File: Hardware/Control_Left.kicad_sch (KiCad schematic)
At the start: 0 parts

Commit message: Schematic review
Initial shcematic iteration.
Added all footprints and part numbers.
Only a quick review was performed.
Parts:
- added C1, C5, C6: 1u, Capacitor_SMD:C_0603_1608Metric, symbol Device:C
- added C2, C4: 4.7u, Capacitor_SMD:C_1206_3216Metric, symbol Device:C
- added C3: 10p, Capacitor_SMD:C_0603_1608Metric, symbol Device:C
- added D1, D2, D3: DSK24, Diode_SMD:D_SOD-123F, symbol Device:D_Schottky
- added J1: BAT, Custom_Parts:JST_PH_1x02_P2.00MM_SMD_HOR, symbol Connector_Generic_MountingPin:Conn_01x02_MountingPin
- added J2: TagConnect, Connector:Tag-Connect_TC2030-IDC-NL_2x03_P1.27mm_Vertical, symbol Connector:Conn_ARM_SWD_TagConnect_TC2030-NL
- added J3: 0.96_TFT_MODULE, Custom_Parts:Jushuo_AFC07-S06FCA-00_1x8-1MP_P0.50_Horizontal, symbol Custom_Parts:0.96_TFT_MODULE
- added L1: 10u, Custom_Parts:VLCF4020, symbol Device:L
- added Q1, Q2: AO3401A, Package_TO_SOT_SMD:SOT-23, symbol Transistor_FET:AO3401A
- added R1: 100K, Resistor_SMD:R_0603_1608Metric, symbol Device:R
- added R2: 500, Resistor_SMD:R_0603_1608Metric, symbol Device:R
- added R3: 470K, Resistor_SMD:R_0603_1608Metric, symbol Device:R
- added R4: 150K, Resistor_SMD:R_0603_1608Metric, symbol Device:R
- added R5: 100, Resistor_SMD:R_0603_1608Metric, symbol Device:R
- added R6, R7: 10K, Resistor_SMD:R_0603_1608Metric, symbol Device:R
- added R8: 22, Resistor_SMD:R_0603_1608Metric, symbol Device:R
- added SW1: MSK12C02, Custom_Parts:MSK12C02, symbol Custom_Parts:MSK12C02
- added U1: TPS61040DBV, Package_TO_SOT_SMD:SOT-23-5, symbol Regulator_Switching:TPS61040DBV
- added U2: XIAO-NRF52840-PLUS, Custom_Parts:XIAO-NRF52840-PLUS-SMD, symbol Custom_Parts:XIAO-NRF52840-PLUS-SMD
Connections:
- new net: C2.1, D1.1 (K), L1.1, Q1.2 (S), U1.5 (VIN)
- new net: D2.2 (A), L1.2, U1.1 (SW)
- new net: C3.2, R3.2, R4.1, U1.3 (FB)
- new net: R2.1, U2.8 (P1.12_RX)
- new net: J1.1 (Pin_1), SW1.2 (B)
- new net: Q2.2 (S), R7.1, R8.1
- new net: J3.1 (LEDA), R8.2
- new net: Q2.1 (G), R5.2, R7.2
- new net 3V3L: C6.1, D3.1 (K), J2.1 (VCC), J3.7 (VDD), Q2.3 (D), R6.1, U2.12 (3V3_OUT)
- new net 5VL: C3.1, C4.1, D2.1 (K), R3.1
- new net COL1_L: U2.1 (P0.02_A0)
- new net COL2_L: U2.2 (P0.03_A1)
- new net COL3_L: U2.3 (P0.28_A2)
- new net COL4_L: U2.4 (P0.29_A3)
- new net COL5_L: U2.5 (P0.04_SDA)
- new net COL6_L: U2.6 (P0.05_SCL)
- new net COL7_L: U2.7 (P1.11_TX)
- new net GND: C1.2, C2.2, C4.2, C5.2, C6.2, J1.2 (Pin_2), J1.MP (MountPin), J2.5 (GND), J3.2 (GND), J3.MP, R1.2, R4.2, SW1.MP, U1.2 (GND), U2.13 (GND), U2.27 (GND), U2.29 (GND)
- new net LCD_BKL: R5.1, U2.21 (P1.03_D17)
- new net LCD_CS: J3.8 (CS), U2.22 (P1.05_D18)
- new net LCD_DC: J3.4 (DC), U2.10 (P1.14_MISO)
- new net LCD_MOSI: J3.5 (SDA), U2.11 (P1.15_MOSI)
- new net LCD_RES: C5.1, D3.2 (A), J3.3 (RES), R6.2
- new net LCD_SCK: J3.6 (SCK), U2.9 (P1.13_SCK)
- new net LED_DATA_L: R2.2
- new net LED_EN: U1.4 (EN), U2.23 (P1.07_D19)
- new net ROW1_L: U2.15 (P0.15_SDOUT)
- new net ROW2_L: U2.16 (P0.19_SCLK)
- new net ROW3_L: U2.17 (P1.01_LRCK)
- new net ROW4_L: U2.18 (P0.09_NFC1)
- new net ROW5_L: U2.19 (P0.10_NFC2)
- new net SWDCLK: J2.4 (SWCLK), U2.25 (SWDCLK)
- new net SWDIO: J2.2 (SWDIO), U2.24 (SWDIO)
- new net VBATL: Q1.3 (D), SW1.3 (C), U2.28 (VBAT)
- new net VBUSL: C1.1, D1.2 (A), Q1.1 (G), R1.1, U2.14 (VBUS)
- new net ~{RESET}: J2.3 (~{RESET}), U2.26 (CHIP_EN)
- no-connect marks 0 -> 3

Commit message: Net configurations
Added net labels.
Updated the PCB components.
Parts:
- removed R2: 500, Resistor_SMD:R_0603_1608Metric, symbol Device:R
- added R1: 500, Resistor_SMD:R_0603_1608Metric, symbol Device:R
- renumbered R1 to R2
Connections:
- net LED_DATA_L: now also R1.2
- net VREGL: now reaches C2.1, D1.1 (K), L1.1, Q1.2 (S), U1.5 (VIN)
- net VSWL: now reaches D2.2 (A), L1.2, U1.1 (SW)
- net VFBL: now reaches C3.2, R3.2, R4.1, U1.3 (FB)
- net LED_DATA: now reaches U2.8 (P1.12_RX)
- net LED_DATA: now also R1.1
- net VBAT: now reaches J1.1 (Pin_1), SW1.2 (B)
- net BKLD: now reaches Q2.2 (S), R7.1, R8.1
- net BKL: now reaches J3.1 (LEDA), R8.2
- net BKLG: now reaches Q2.1 (G), R5.2, R7.2
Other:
- moved on the sheet: R5, R8

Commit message: Initial layout
Configured the switch and LED initial layout.
Need to add the capacitors for the LEDs and the diodes for the switches.
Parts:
- added R3: 10K, Resistor_SMD:R_0603_1608Metric, symbol Device:R
- renumbered R3 to R4, R4 to R5, R5 to R6, R6 to R7, R7 to R8, R8 to R9
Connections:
- net COL7_L is gone; now on net LED_EN: U2.7 (P1.11_TX)
- net GND: now also R3.1
- net LED_EN: now also R3.2; no longer U2.23 (P1.07_D19)
- new net ROW6_L: U2.23 (P1.07_D19)

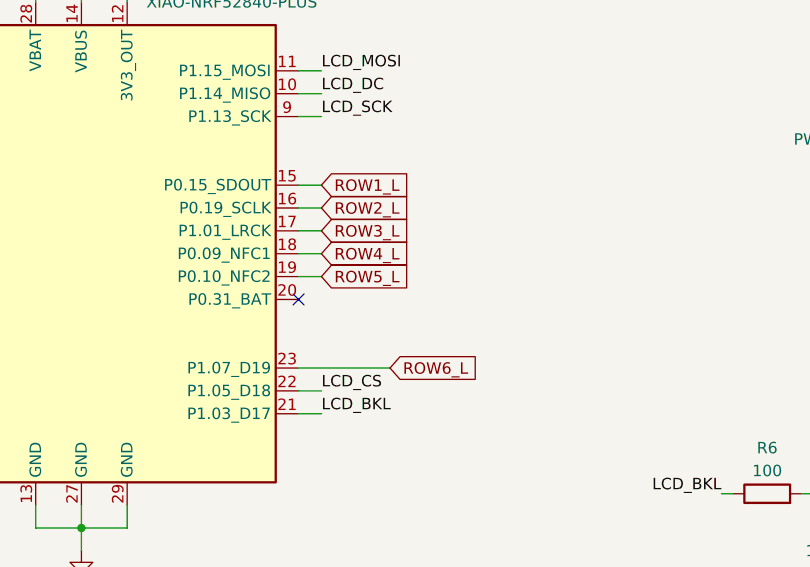
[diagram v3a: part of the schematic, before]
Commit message: Pin adjustment
Adjusted the pins for the encoders and other.
Now the battery measuring pin connected to an internal ADC on the XIAO nRF52840 also serves to read the rotation of the encoders.
Attention should be put as how to implement the BAT voltage measuring to check if the encoder is turning at the same time.
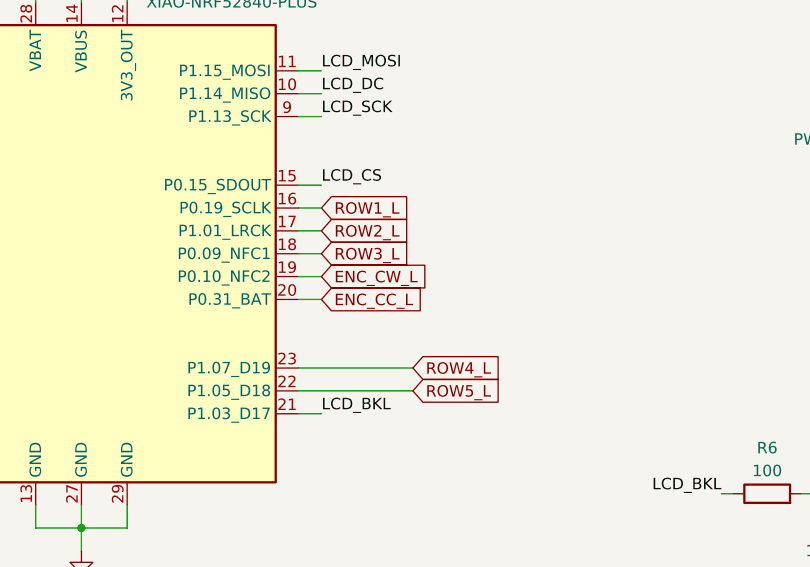
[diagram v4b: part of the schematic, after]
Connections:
- net ROW6_L is gone; now on net ROW4_L: U2.23 (P1.07_D19)
- net LCD_CS: now also U2.15 (P0.15_SDOUT); no longer U2.22 (P1.05_D18)
- net ROW1_L: now also U2.16 (P0.19_SCLK); no longer U2.15 (P0.15_SDOUT)
- net ROW2_L: now also U2.17 (P1.01_LRCK); no longer U2.16 (P0.19_SCLK)
- net ROW3_L: now also U2.18 (P0.09_NFC1); no longer U2.17 (P1.01_LRCK)
- net ROW4_L: no longer U2.18 (P0.09_NFC1)
- net ROW5_L: now also U2.22 (P1.05_D18); no longer U2.19 (P0.10_NFC2)
- net ENC_CC_L: now reaches U2.20 (P0.31_BAT)
- new net ENC_CW_L: U2.19 (P0.10_NFC2)
- no-connect marks 3 -> 2

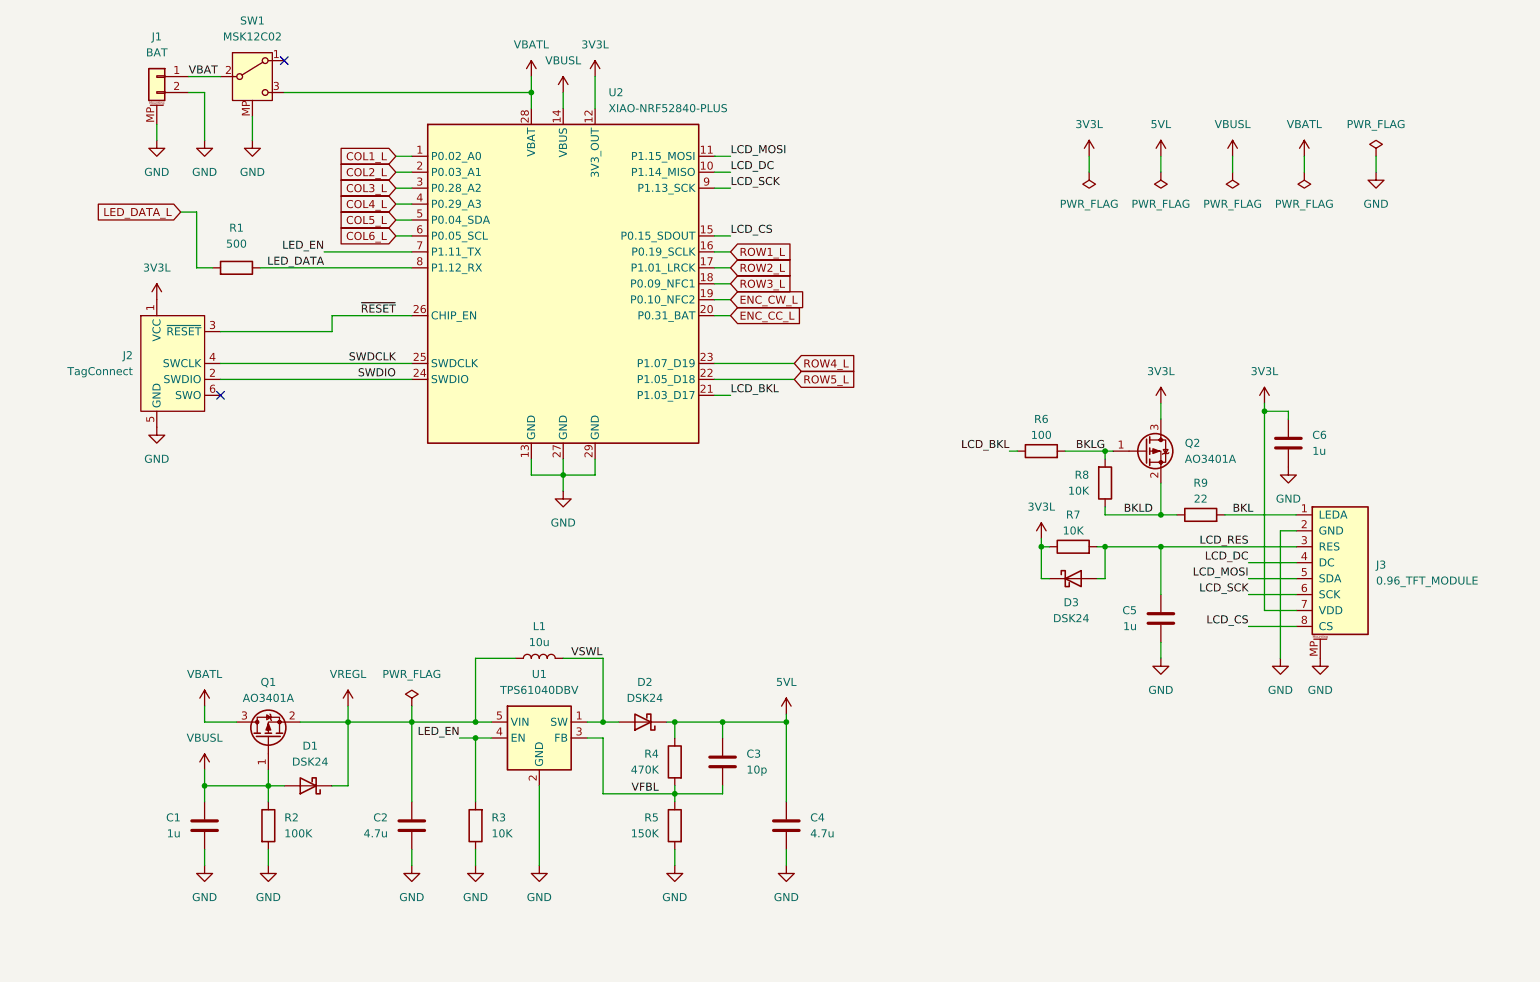
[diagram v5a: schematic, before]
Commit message: Key matrix and edges
Defined the key matrix locations and the board edges.
Next step: start routing and verify the buck converter layout.
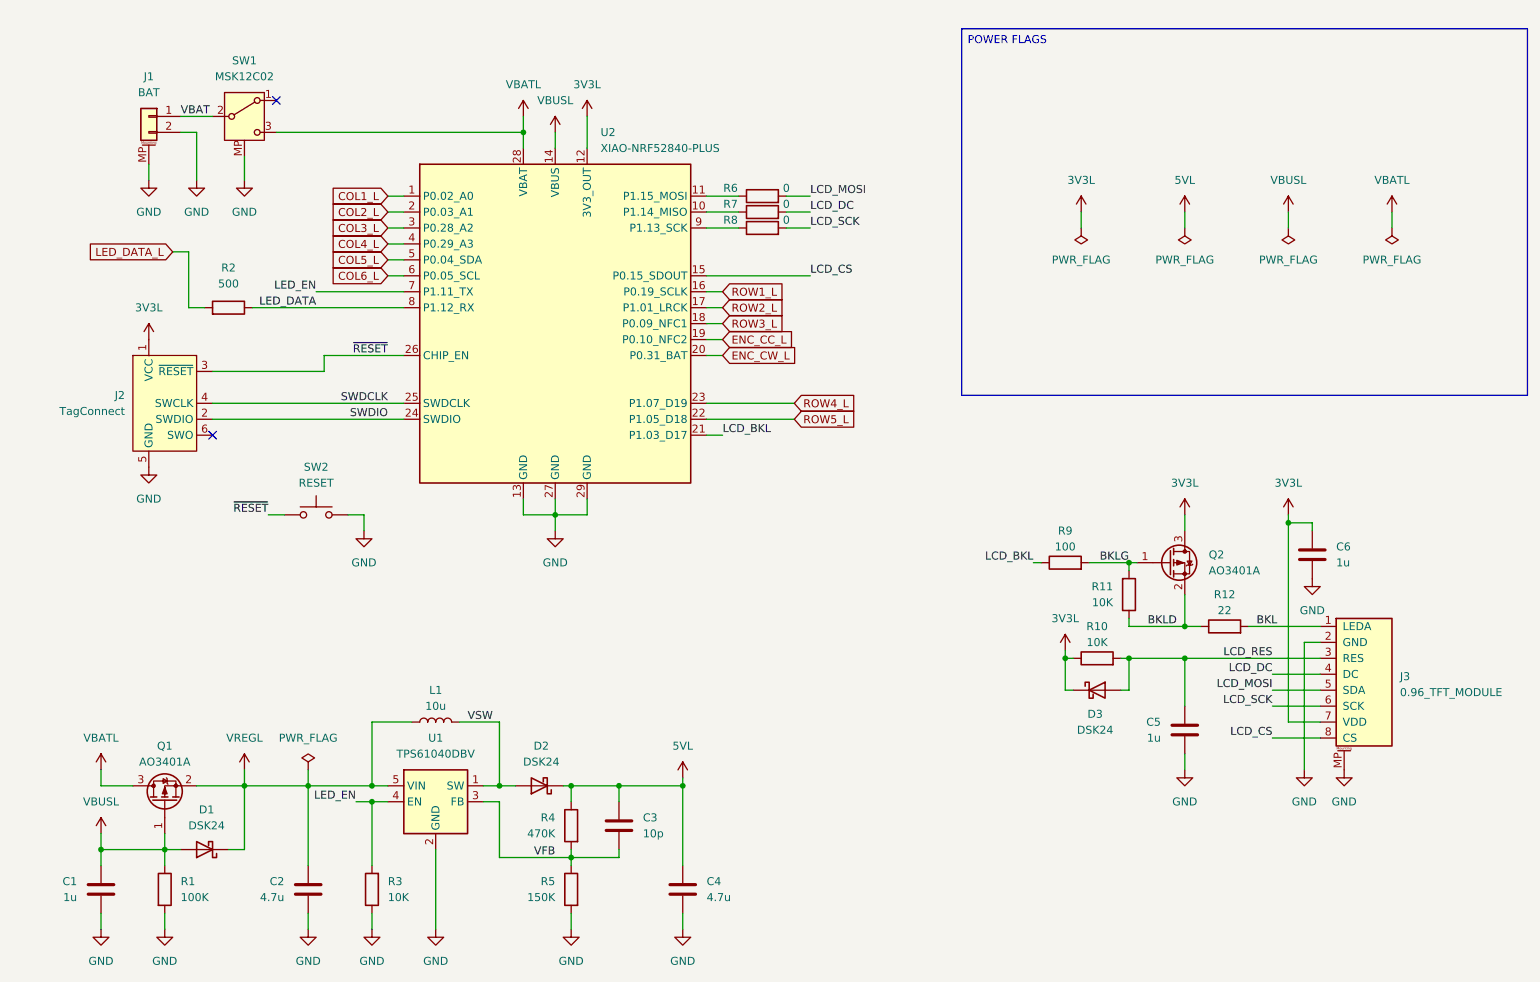
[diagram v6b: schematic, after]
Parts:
- added R10, R11: 10K, Resistor_SMD:R_0603_1608Metric, symbol Device:R
- added R12: 22, Resistor_SMD:R_0603_1608Metric, symbol Device:R
- added SW2: RESET, Button_Switch_SMD:SW_SPST_TS-1088-xR020, symbol Switch:SW_Push
- J3: footprint Custom_Parts:Jushuo_AFC07-S06FCA-00_1x8-1MP_P0.50_Horizontal -> Custom_Parts:0.96_TFT_MODULE
- L1: footprint Custom_Parts:VLCF4020 -> Custom_Parts:VLCF4020_MIRROR
- R1: value 500 -> 100K; JLC Part 0603WAF5100T5E -> C25803; Manufacturer Part 0603WAF5100T5E -> 0603WAF1003T5E
- R2: value 100K -> 500; JLC Part C25803 -> 0603WAF5100T5E; Manufacturer Part 0603WAF1003T5E -> 0603WAF5100T5E
- R6: value 100 -> 0; JLC Part 0603WAF1000T5E -> C21189; Manufacturer Part 0603WAF1000T5E -> 0603WAF0000T5E
- R7, R8: value 10K -> 0; JLC Part 0603WAF1002T5E -> C21189; Manufacturer Part 0603WAF1002T5E -> 0603WAF0000T5E
- R9: value 22 -> 100; JLC Part C23345 -> 0603WAF1000T5E; Manufacturer Part 0603WAF220JT5E -> 0603WAF1000T5E
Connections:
- net 3V3L: now also R10.1; no longer R7.1
- net BKL: now also R12.2; no longer R9.2
- net BKLD: now also R11.1, R12.1; no longer R8.1, R9.1
- net BKLG: now also R9.2, R11.2; no longer R6.2, R8.2
- net ENC_CC_L: now also U2.19 (P0.10_NFC2); no longer U2.20 (P0.31_BAT)
- net ENC_CW_L: now also U2.20 (P0.31_BAT); no longer U2.19 (P0.10_NFC2)
- net GND: now also R1.2, SW2.2; no longer R2.2
- net LCD_BKL: now also R9.1; no longer R6.1
- net LCD_DC: now also R7.2; no longer U2.10 (P1.14_MISO)
- net LCD_MOSI: now also R6.2; no longer U2.11 (P1.15_MOSI)
- net LCD_RES: now also R10.2; no longer R7.2
- net LCD_SCK: now also R8.2; no longer U2.9 (P1.13_SCK)
- net LED_DATA: now also R2.1; no longer R1.1
- net LED_DATA_L: now also R2.2; no longer R1.2
- net VBUSL: now also R1.1; no longer R2.1
- net ~{RESET}: now also SW2.1
- net VFBL renamed VFB
- net VSWL renamed VSW
- new net: R8.1, U2.9 (P1.13_SCK)
- new net: R7.1, U2.10 (P1.14_MISO)
- new net: R6.1, U2.11 (P1.15_MOSI)

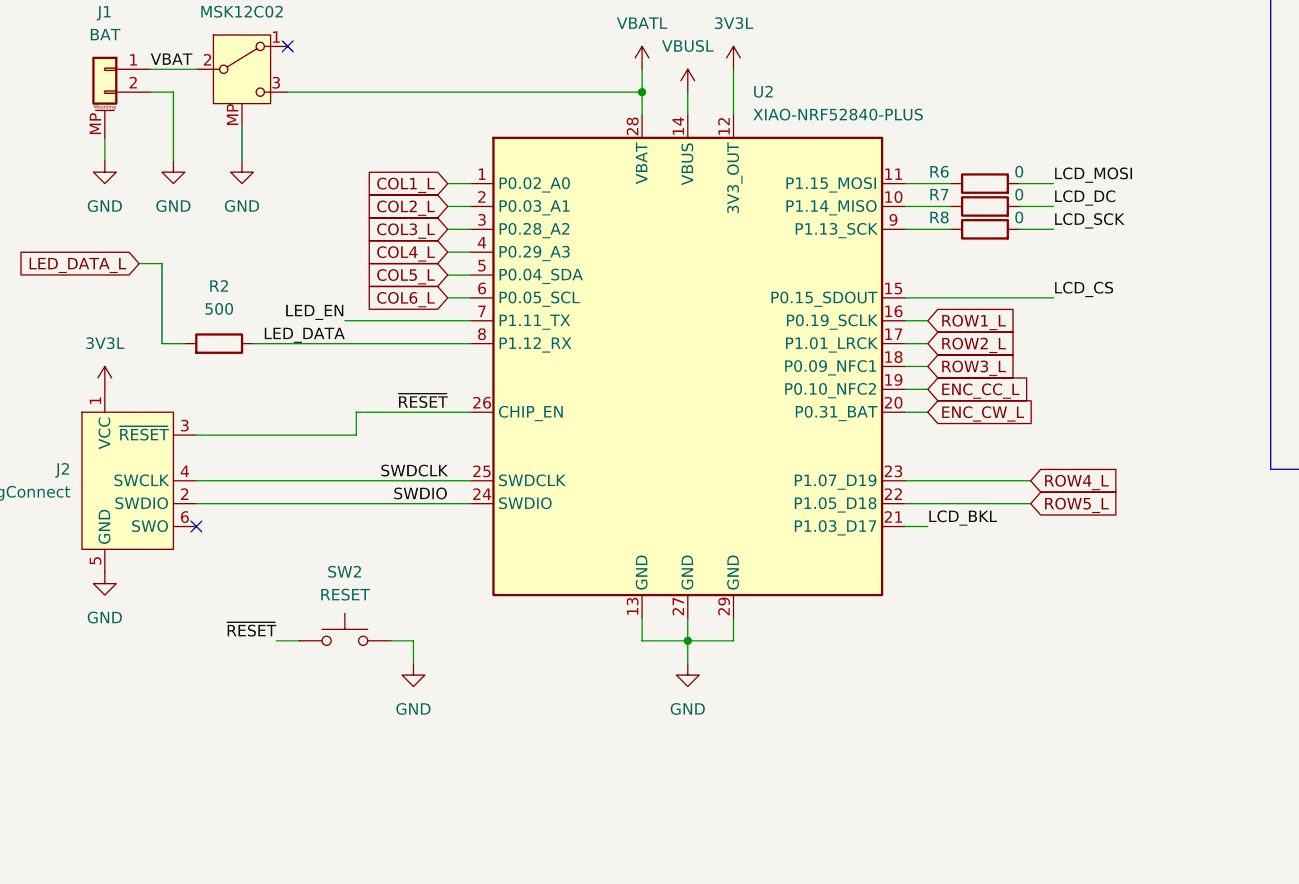
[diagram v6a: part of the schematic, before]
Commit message: Pinout and footprints
Updated the MCU footprints because the silkscreen was too close to the edge.
Updated the pinout for the MCUs. The left side seems to be ok, but the right side may need some adjustments.
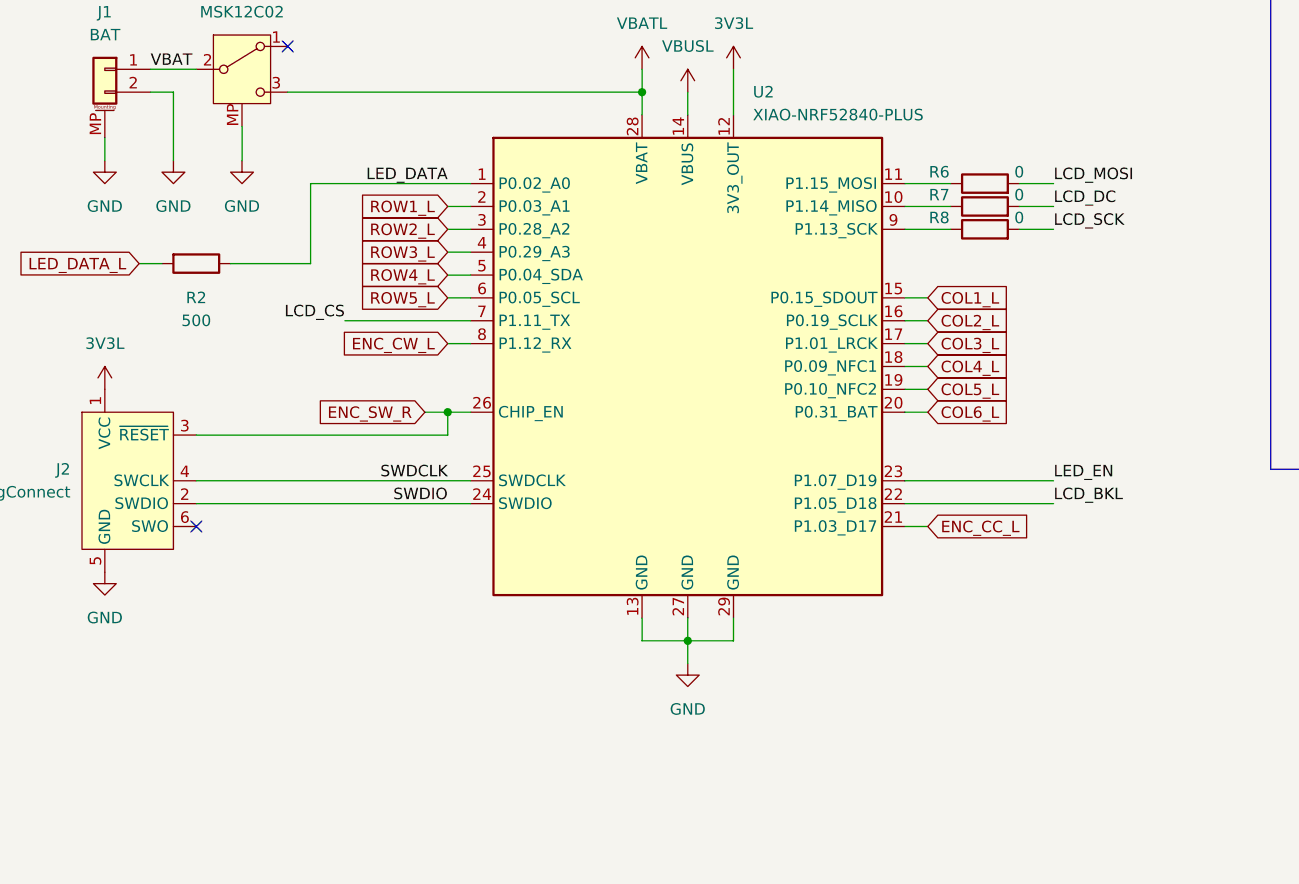
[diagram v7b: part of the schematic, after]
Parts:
- removed SW2: RESET, Button_Switch_SMD:SW_SPST_TS-1088-xR020, symbol Switch:SW_Push
- U2: footprint Custom_Parts:XIAO-NRF52840-PLUS-SMD -> Custom_Parts:XIAO-NRF52840-PLUS-SMD-EDGE
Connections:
- net COL1_L: now also U2.15 (P0.15_SDOUT); no longer U2.1 (P0.02_A0)
- net COL2_L: now also U2.16 (P0.19_SCLK); no longer U2.2 (P0.03_A1)
- net COL3_L: now also U2.17 (P1.01_LRCK); no longer U2.3 (P0.28_A2)
- net COL4_L: now also U2.18 (P0.09_NFC1); no longer U2.4 (P0.29_A3)
- net COL5_L: now also U2.19 (P0.10_NFC2); no longer U2.5 (P0.04_SDA)
- net COL6_L: now also U2.20 (P0.31_BAT); no longer U2.6 (P0.05_SCL)
- net ENC_CC_L: now also U2.21 (P1.03_D17); no longer U2.19 (P0.10_NFC2)
- net ENC_CW_L: now also U2.8 (P1.12_RX); no longer U2.20 (P0.31_BAT)
- net LCD_BKL: now also U2.22 (P1.05_D18); no longer U2.21 (P1.03_D17)
- net LCD_CS: now also U2.7 (P1.11_TX); no longer U2.15 (P0.15_SDOUT)
- net LED_DATA: now also U2.1 (P0.02_A0); no longer U2.8 (P1.12_RX)
- net LED_EN: now also U2.23 (P1.07_D19); no longer U2.7 (P1.11_TX)
- net ROW1_L: now also U2.2 (P0.03_A1); no longer U2.16 (P0.19_SCLK)
- net ROW2_L: now also U2.3 (P0.28_A2); no longer U2.17 (P1.01_LRCK)
- net ROW3_L: now also U2.4 (P0.29_A3); no longer U2.18 (P0.09_NFC1)
- net ROW4_L: now also U2.5 (P0.04_SDA); no longer U2.23 (P1.07_D19)
- net ROW5_L: now also U2.6 (P0.05_SCL); no longer U2.22 (P1.05_D18)
- net ~{RESET} renamed ENC_SW_R
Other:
- moved on the sheet: R2
